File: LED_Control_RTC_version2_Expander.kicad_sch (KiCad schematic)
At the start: 89 parts, among them J10 Conn_01x06_Male, J210 Conn_01x02, J220 Conn_01x02, J230 Conn_01x02, J240 Conn_01x02, J250 Conn_01x02, J260 Conn_01x02, J3 Conn_02x04_Odd_Even, J4 DS1023-2*8SF11, J5 DS1023-2*8SF11, J9 Conn_01x06_Male, Q1 IRLR8726TRPBF, Q10 IRLR8726TRPBF, Q2 IRLR8726TRPBF, Q3 IRLR8726TRPBF, Q4 IRLR8726TRPBF, Q5 IRLR8726TRPBF, Q6 IRLR8726TRPBF, Q7 IRLR8726TRPBF, Q8 IRLR8726TRPBF, Q9 IRLR8726TRPBF, U101 TC4427, U102 TC4427, U103 TC4427, U104 TC4427, U105 TC4427

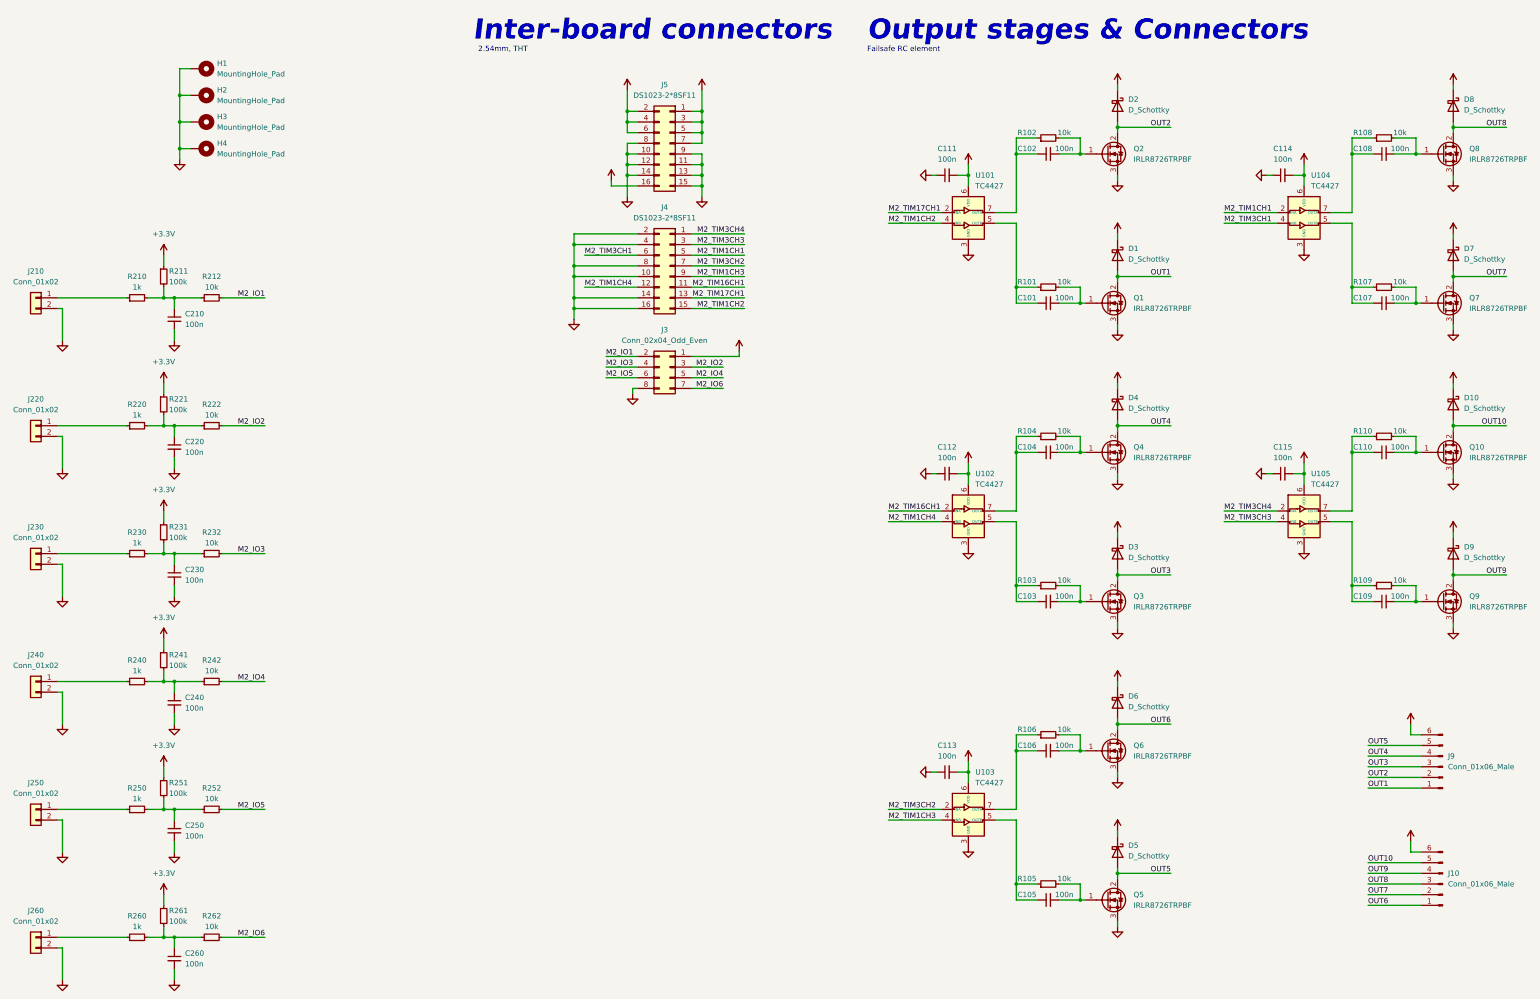
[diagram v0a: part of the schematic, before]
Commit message: Added ESD protection to switch inputs and filled planes
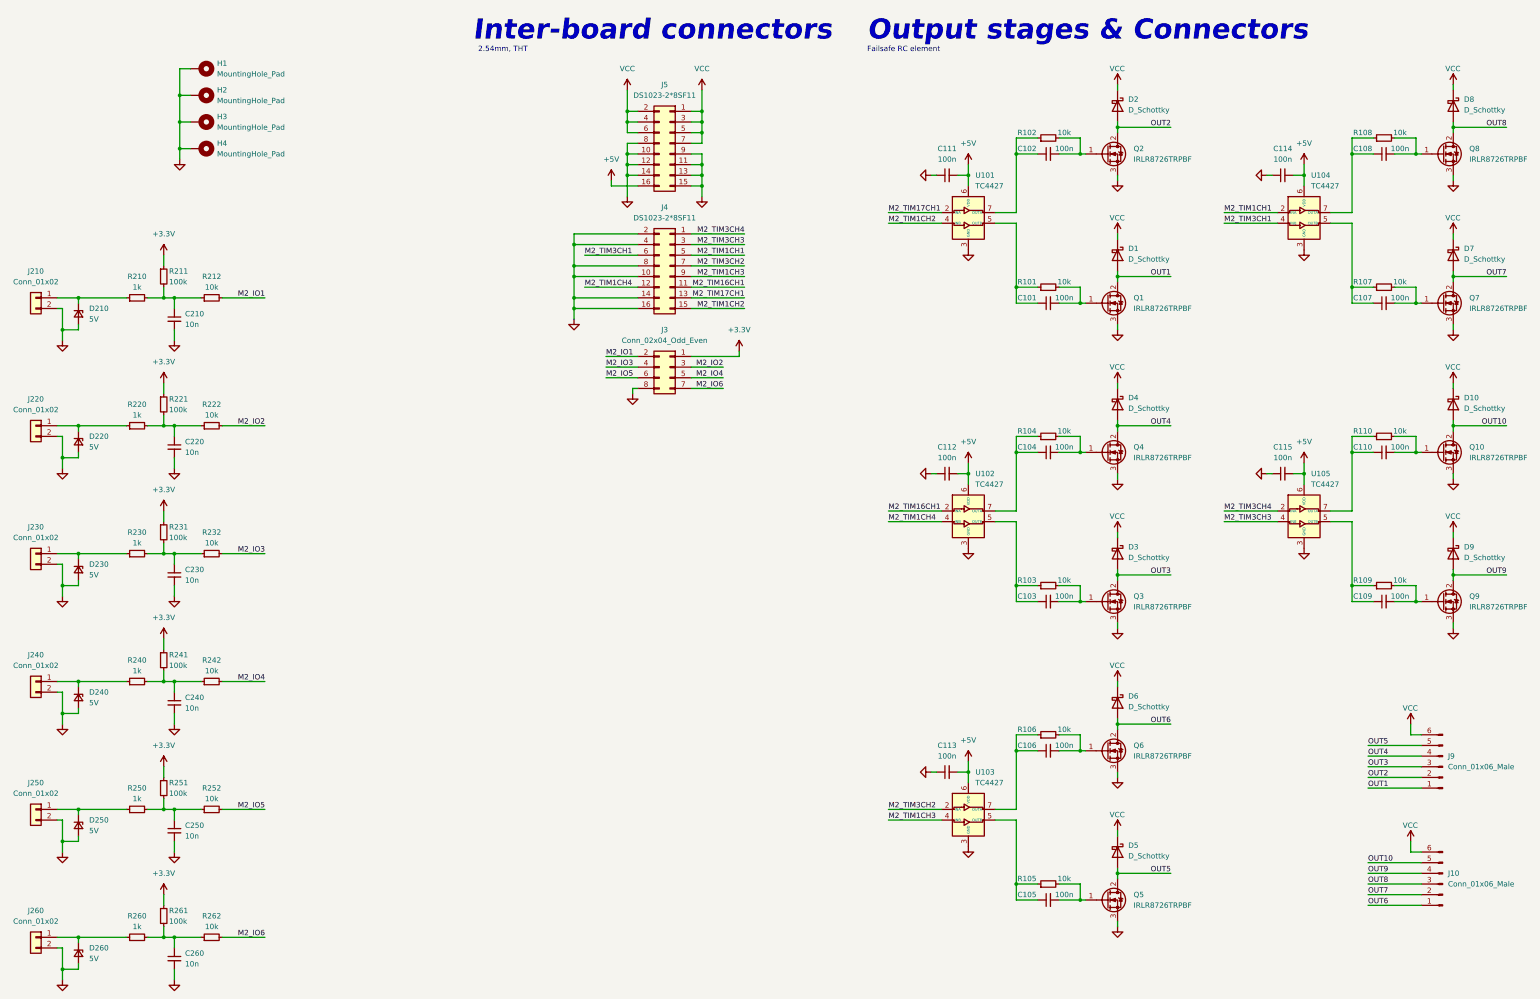
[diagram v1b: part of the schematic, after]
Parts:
- added D210, D220, D230, D240, D250, D260: 5V, Diode_SMD:D_SOD-323, symbol Device:D_Zener_Small
- C210, C220, C230, C240, C250, C260: value 100n -> 10n; footprint Capacitor_SMD:C_0603_1608Metric -> Capacitor_SMD:C_0402_1005Metric
- R210, R211, R212, R220, R221, R222, R230, R231, R232, R240, R241, R242, R250, R251, R252, R260, R261, R262: footprint Resistor_SMD:R_0603_1608Metric -> Resistor_SMD:R_0402_1005Metric
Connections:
- net GND: now also D210.2 (A), D220.2 (A), D230.2 (A), D240.2 (A), D250.2 (A), D260.2 (A)
- net at J260.1 (Pin_1), R260.1: now also D260.1 (K)
- net at J230.1 (Pin_1), R230.1: now also D230.1 (K)
- net at J250.1 (Pin_1), R250.1: now also D250.1 (K)
- net at J210.1 (Pin_1), R210.1: now also D210.1 (K)
- net at J220.1 (Pin_1), R220.1: now also D220.1 (K)
- net at J240.1 (Pin_1), R240.1: now also D240.1 (K)

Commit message: Finished design
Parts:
- added C100: 10u, Resistor_SMD:R_1206_3216Metric, symbol Device:C_Small
- added C200, C201: 100n, Capacitor_SMD:C_0402_1005Metric, symbol Device:C_Small
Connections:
- net +3V3: now also C200.1, C201.1
- net +5V: now also C100.1
- net GND: now also C100.2, C200.2, C201.2
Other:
- note added: "2.54mm Terminal block"
- note added: "Switch input connectors"
- moved on the sheet: C210, C220, C230, C240, C250, C260, D210, D220, D230, D240, D250, D260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
